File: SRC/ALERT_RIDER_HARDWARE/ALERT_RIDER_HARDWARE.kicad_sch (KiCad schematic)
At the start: 50 parts, among them J1 Screw_Terminal_01x02, J3 USB_C_Receptacle_USB2.0, J4 THERMISTOR, Q1 IRLML5203TRPBF, Q6 IRLML0100TRPBF, U3 TPS63802DLAR, U5 LORA-E32-915T30S

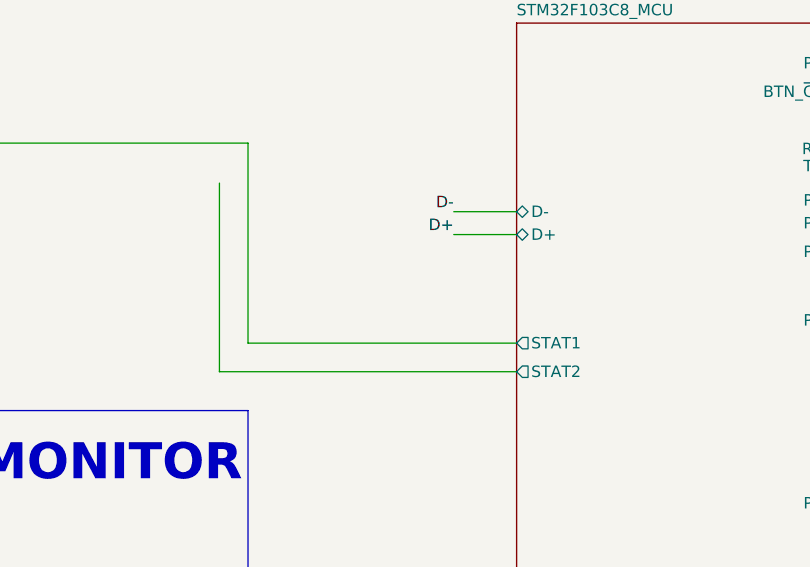
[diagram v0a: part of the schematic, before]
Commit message: complete Pa8-Pa7 LED placement maximized all files generated
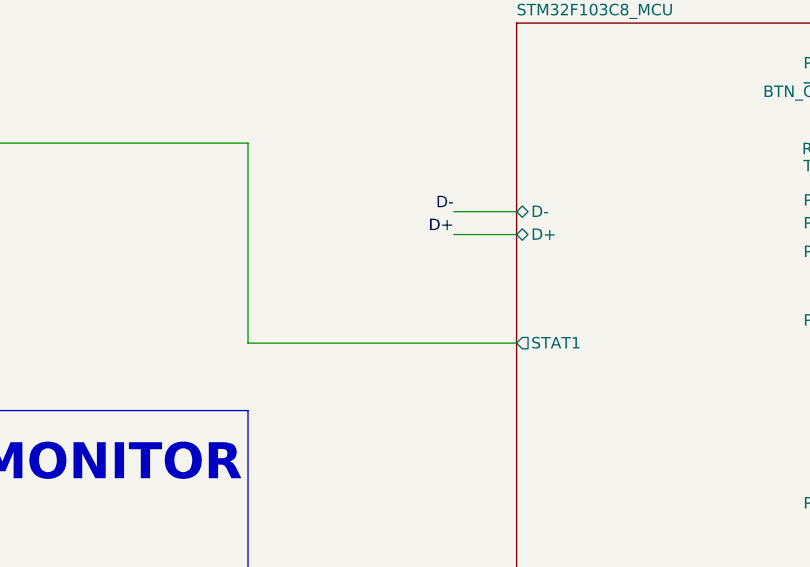
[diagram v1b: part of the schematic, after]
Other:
- sheet STM32F103C8_MCU ports: added none; removed STAT2
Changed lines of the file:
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@@
-    (stroke (width 0) (type default))
-  )
-  (wire (pts (xy 193.04 181.61) (xy 193.04 160.655))
     (stroke (width 0) (type default))
   )
@@
   )
   (wire (pts (xy 68.58 71.755) (xy 69.85 71.755))
-    (stroke (width 0) (type default))
-  )
-  (wire (pts (xy 226.06 181.61) (xy 193.04 181.61))
     (stroke (width 0) (type default))
   )
@@
       (effects (font (size 1.27 1.27)) (justify right))
     )
-    (pin "STAT2" output (at 226.06 181.61 180)
-      (effects (font (size 1.27 1.27)) (justify left))
-    )
     (pin "STAT1" output (at 226.06 178.435 180)
